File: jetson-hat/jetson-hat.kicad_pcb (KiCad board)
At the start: 2 copper layers, 65 x 56 mm, 5 parts, among them J1 GPIO

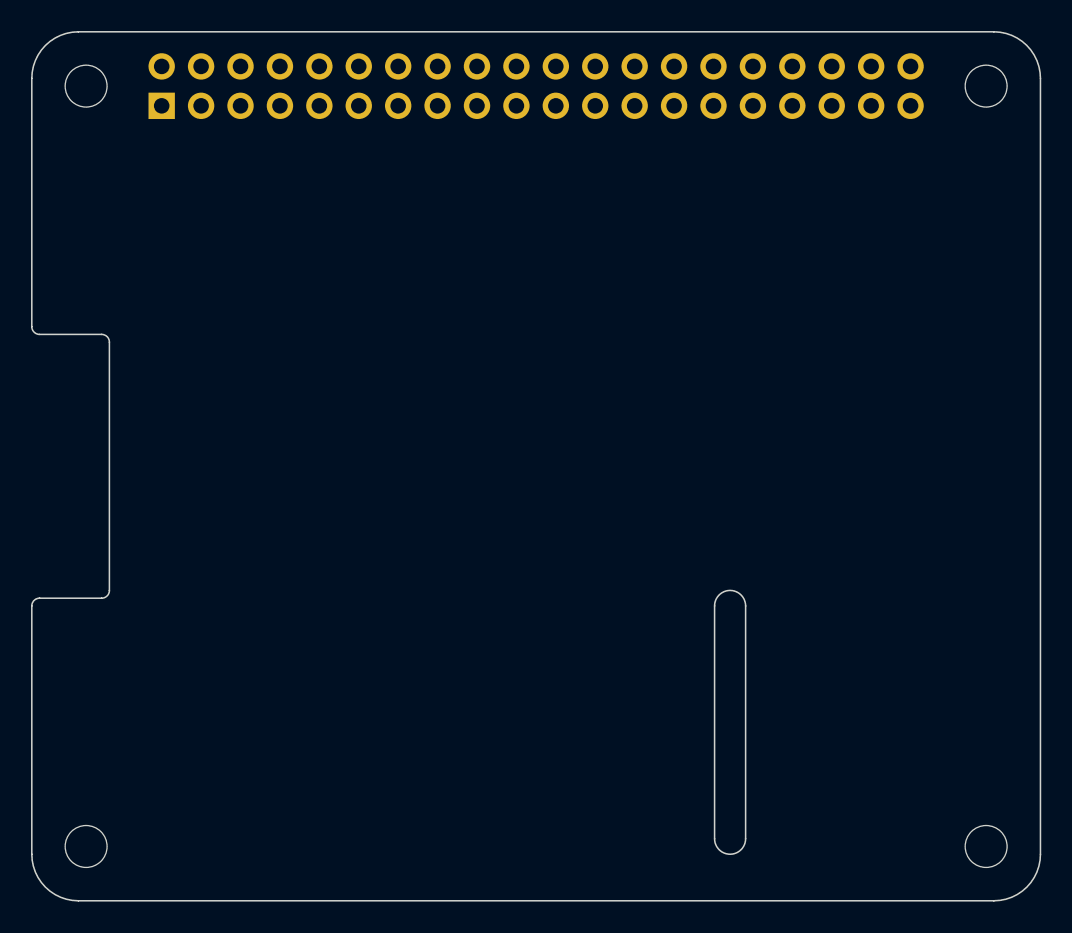
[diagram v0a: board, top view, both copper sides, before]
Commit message: Begin layout for Jetson
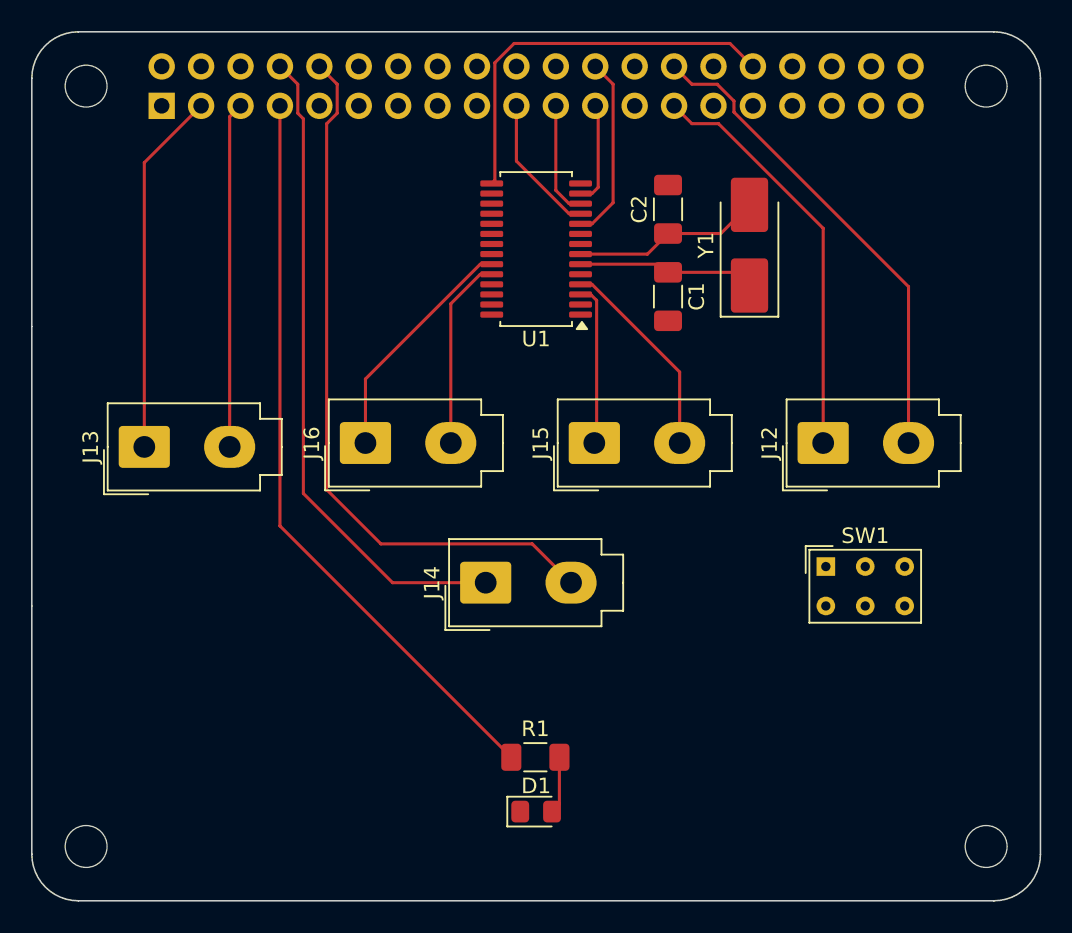
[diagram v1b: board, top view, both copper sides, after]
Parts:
- added C1: 22pF, Capacitor_SMD:C_1206_3216Metric_Pad1.33x1.80mm_HandSolder, F.Cu at (141.0, 61.1)
- added C2: 33pF, Capacitor_SMD:C_1206_3216Metric_Pad1.33x1.80mm_HandSolder, F.Cu at (141.0, 55.4)
- added D1: LED, LED_SMD:LED_0805_2012Metric_Pad1.15x1.40mm_HandSolder, F.Cu at (132.5, 94.2)
- added J12: Conn_01x02_Pin, Connector_Molex:Molex_Mini-Fit_Jr_5566-02A_2x01_P4.20mm_Vertical, F.Cu at (151.0, 70.5)
- added J13: Conn_01x02_Pin, Connector_Molex:Molex_Mini-Fit_Jr_5566-02A_2x01_P4.20mm_Vertical, F.Cu at (107.2, 70.8)
- added J14: Conn_01x02_Pin, Connector_Molex:Molex_Mini-Fit_Jr_5566-02A_2x01_P4.20mm_Vertical, F.Cu at (129.2, 79.5)
- added J15: Conn_01x02_Pin, Connector_Molex:Molex_Mini-Fit_Jr_5566-02A_2x01_P4.20mm_Vertical, F.Cu at (136.2, 70.5)
- added J16: Conn_01x02_Pin, Connector_Molex:Molex_Mini-Fit_Jr_5566-02A_2x01_P4.20mm_Vertical, F.Cu at (121.5, 70.5)
- added R1: 150, Resistor_SMD:R_1206_3216Metric_Pad1.30x1.75mm_HandSolder, F.Cu at (132.4, 90.8)
- added SW1: SW_Push, Button_Switch_THT:SW_NKK_GW12LJP, F.Cu at (151.2, 78.5)
- added U1: SC16IS752IPW, Package_SO:TSSOP-28_4.4x9.7mm_P0.65mm, F.Cu at (132.5, 58.0)
- added Y1: Crystal, Crystal:Crystal_SMD_5032-2Pin_5.0x3.2mm_HandSoldering, F.Cu at (146.2, 57.8)
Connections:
- net /GPIO22 renamed /jetson-board/PIN15/GPIO12
- net /GPIO23 renamed /jetson-board/PIN16/CS1-1
- net /GPIO24 renamed /jetson-board/PIN18/CS1-0
- net /GPIO25 renamed /jetson-board/PIN22/MISO1
- net /GPIO26 renamed /jetson-board/PIN37/MOSI1
- net /GPIO27 renamed /jetson-board/PIN13/SCK1
- net /GPIO5 renamed /jetson-board/PIN29/GPIO1
- net /GPIO7/SPI0.CE1 renamed /jetson-board/PIN26/CS0-1
- J1 pad 10: /GPIO15/RXD0 -> /jetson-board/PIN10/RXD1
- J1 pad 11: /GPIO17 -> unconnected-(J1-Pin_11-Pad11)
- J1 pad 12: /GPIO18/PCM.CLK -> unconnected-(J1-Pin_12-Pad12)
- J1 pad 14: GND -> unconnected-(J1-Pin_14-Pad14)
- J1 pad 17: +3V3 -> unconnected-(J1-Pin_17-Pad17)
- J1 pad 19: /GPIO10/SPI0.MOSI -> /jetson-board/PIN19/MOSI0
- J1 pad 2: +5V -> unconnected-(J1-Pin_2-Pad2)
- J1 pad 20: GND -> unconnected-(J1-Pin_20-Pad20)
- J1 pad 21: /GPIO9/SPI0.MISO -> /jetson-board/PIN21/MISO0
- J1 pad 23: /GPIO11/SPI0.SCLK -> /jetson-board/PIN23/SCK0
- J1 pad 24: /GPIO8/SPI0.CE0 -> /jetson-board/PIN24/CS0-0
- J1 pad 25: GND -> unconnected-(J1-Pin_25-Pad25)
- J1 pad 27: /ID_SDA -> /jetson-board/PIN27/SDA0
- J1 pad 28: /ID_SCL -> /jetson-board/PIN28/SCL0
- J1 pad 3: /GPIO2/SDA1 -> /jetson-board/PIN3/SDA1
- J1 pad 30: GND -> unconnected-(J1-Pin_30-Pad30)
- J1 pad 31: /GPIO6 -> /jetson-board/PIN31/GPIO11/RST
- J1 pad 32: /GPIO12/PWM0 -> /jetson-board/PIN32/GPIO7/IRQ
- J1 pad 33: /GPIO13/PWM1 -> /jetson-board/PIN33/GPIO13/BUTTON
- J1 pad 34: GND -> unconnected-(J1-Pin_34-Pad34)
- J1 pad 35: /GPIO19/PCM.FS -> unconnected-(J1-Pin_35-Pad35)
- J1 pad 36: /GPIO16 -> unconnected-(J1-Pin_36-Pad36)
- J1 pad 38: /GPIO20/PCM.DIN -> unconnected-(J1-Pin_38-Pad38)
- J1 pad 39: GND -> unconnected-(J1-Pin_39-Pad39)
- J1 pad 4: +5V -> unconnected-(J1-Pin_4-Pad4)
- J1 pad 40: /GPIO21/PCM.DOUT -> unconnected-(J1-Pin_40-Pad40)
- J1 pad 5: /GPIO3/SCL1 -> /jetson-board/PIN5/SCL1
- J1 pad 7: /GPIO4/GPCLK0 -> /jetson-board/PIN7/GPIO9/LED0
- J1 pad 8: /GPIO14/TXD0 -> /jetson-board/PIN8/TXD1
- J1 pad 9: GND -> unconnected-(J1-Pin_9-Pad9)
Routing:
- net /jetson-board/PIN7/GPIO9/LED0: track 0.00 -> 48.2 mm
- net /jetson-board/PIN10/RXD1: track 0.00 -> 46.3 mm
- net /jetson-board/PIN8/TXD1: track 0.00 -> 42.3 mm
- net /jetson-board/PIN28/SCL0: track 0.00 -> 31.5 mm
- net /jetson-board/PIN27/SDA0: track 0.00 -> 26.7 mm
- net /jetson-board/PIN32/GPIO7/IRQ: track 0.00 -> 25.6 mm
- net /jetson-board/PIN3/SDA1: track 0.00 -> 23.5 mm
- net /jetson-board/PIN5/SCL1: track 0.00 -> 22.3 mm
- net /jetson-board/TXB: track 0.00 -> 15.3 mm
- net /jetson-board/RXA: track 0.00 -> 13.3 mm
- net /jetson-board/RXB: track 0.00 -> 12.4 mm
- net Net-(U1-XTAL2): track 0.00 -> 12.2 mm
- net /jetson-board/PIN24/CS0-0: track 0.00 -> 11.9 mm
- net Net-(U1-XTAL1): track 0.00 -> 11.5 mm
- net /jetson-board/TXA: track 0.00 -> 10.5 mm
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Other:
- outline, holes or cut-outs redrawn
- board text removed: "CAMERA (OPTIONAL)"
- board text removed: "DISPLAY (OPTIONAL)"
- board text removed: "PoE"
- board text removed: "RJ45"
- board text removed: "USB"
